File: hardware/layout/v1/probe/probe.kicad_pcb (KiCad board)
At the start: 4 copper layers, 14 x 50 mm, 19 parts, among them J1 Main board, J2 Reflector T-Socket SMD, Q1 AO3400A, U1 SCD41-D-R2, U2 SGP41-D-R4, U3 SHT45-AD1F-R2, U4 LM393DR2G

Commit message: Update documentation to reflect hardware specification changes and component substitutions
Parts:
- U3: value SHT45-AD1F-R2 -> SHT40-AD1F-R2

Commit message: Add silkscreen connector labels to all PCB variants for improved assembly identification
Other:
- board text added: "MAIN"
- board text added: "REFLECTOR"

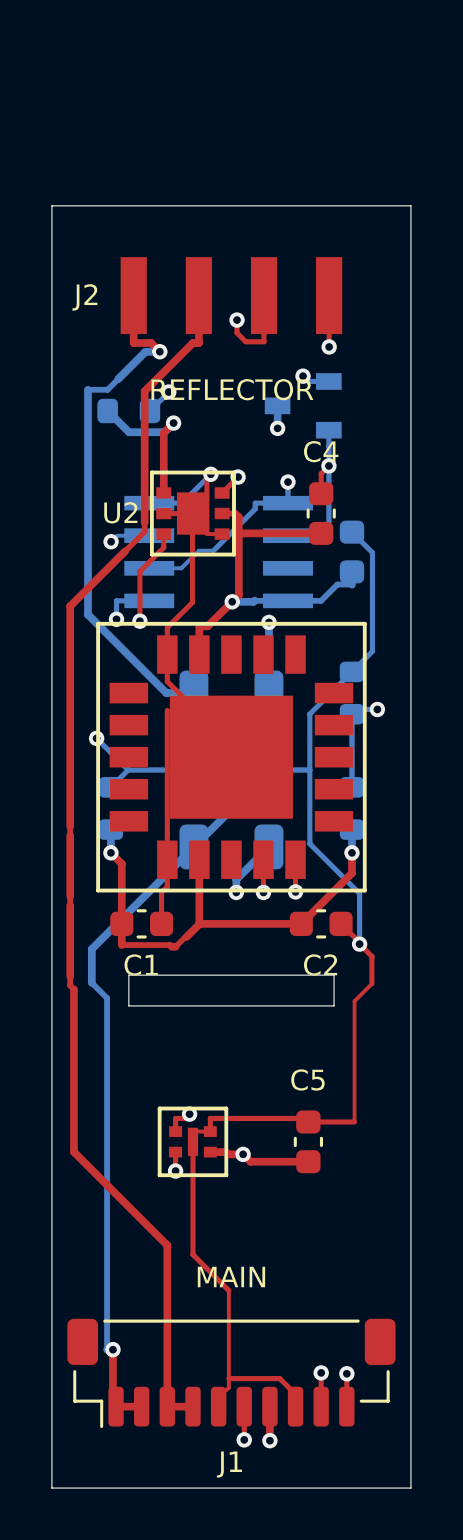
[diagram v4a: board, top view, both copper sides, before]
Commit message: Update enclosure dimensions, add power board, upgrade sensors, and redesign base bay for PMSA003I particulate module
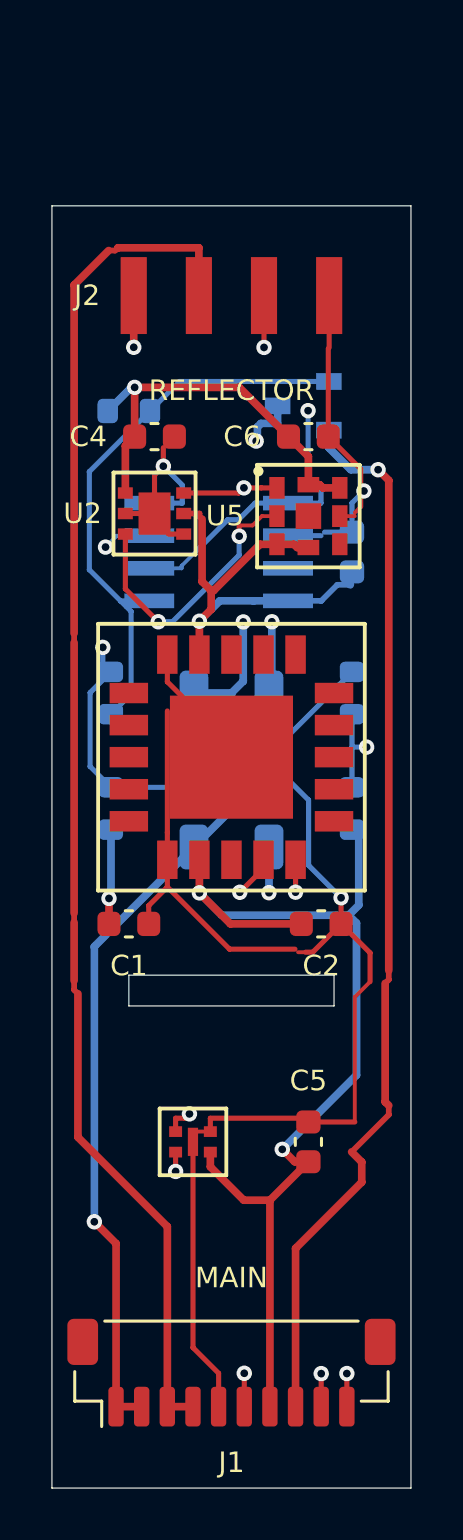
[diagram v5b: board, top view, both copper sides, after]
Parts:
- added C6: 100n 50V, Capacitor_SMD:C_0603_1608Metric, F.Cu at (10.0, -41.0)
- added R7: 470k, Resistor_SMD:R_0603_1608Metric, B.Cu at (2.30, -31.0)
- added U5: BMP585, gateway_fp:Bosch_BMP585_LGA-9, F.Cu at (10.0, -37.9)
- R1, R2: value 470R -> 120R
- moved C4 7.16 mm to (4.00, -41.0), turned to 0 degrees
- moved U2 1.50 mm to (4.00, -38.0)
- moved C1 0.50 mm to (3.00, -22.0)
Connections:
- net VIN_PROT renamed +5V_HEAT
- J1 pad 8: GND -> CO2_HEAT_RTN
- Q1 pad 2: GND -> CO2_HEAT_RTN
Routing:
- net CO2_HEAT_RTN: track 0.00 -> 41.6 mm, vias 0 -> 1
- net I2C_SDA: track 49.8 -> 61.3 mm, vias 4 -> 5
- net I2C_SCL: track 51.0 -> 58.9 mm
- net CO2_VSET: track 21.6 -> 29.1 mm
- net CO2_HEAT_SW: track 34.0 -> 28.0 mm
- net HEAT_SW: track 48.1 -> 53.6 mm
- net +3V3: track 105.7 -> 103.0 mm, vias 6 -> 5
- net NTC_SENSE: track 55.9 -> 53.6 mm
- net +5V_HEAT: track 52.8 -> 53.7 mm, vias 2 -> 3
- net CO2_NTC: track 15.4 -> 16.3 mm
- net GND: track 79.4 -> 78.7 mm, vias 4 -> 3
- net CO2_GATE: track 23.1 -> 22.4 mm, vias 3 -> 0

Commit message: Update documentation for 60V power system, STM32 crown board, 12V heaters, and expanded enclosure design
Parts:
- R1, R2: value 120R -> 680R
- U4: value LM393DR2G -> LM2903DR2G
- moved J2 6.00 mm to (7.00, -52.5)
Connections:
- C3 pad 1: +3V3 -> +12V_HEAT
- J1 pad 1: +5V_HEAT -> +12V_HEAT
- J1 pad 2: +5V_HEAT -> +12V_HEAT
- J2 pad 1: +5V_HEAT -> +12V_HEAT
- R1 pad 1: +5V_HEAT -> +12V_HEAT
- R2 pad 1: +5V_HEAT -> +12V_HEAT
- U4 pad 8: +3V3 -> +12V_HEAT
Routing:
- net +12V_HEAT: track 0.00 -> 63.3 mm, vias 0 -> 3
- net +5V_HEAT: track 53.7 -> 0.00 mm, vias 3 -> 0
- net GND: track 78.7 -> 97.4 mm, vias 3 -> 4
- net I2C_SCL: track 58.9 -> 75.6 mm
- net +3V3: track 103.0 -> 114.4 mm
- net CO2_HEAT_SW: track 28.0 -> 18.1 mm, vias 3 -> 2
- net CO2_VSET: track 29.1 -> 24.1 mm, vias 2 -> 0
- net CO2_GATE: track 22.4 -> 27.2 mm, vias 0 -> 2
- net NTC_SENSE: track 53.6 -> 56.1 mm
- net I2C_SDA: track 61.3 -> 62.3 mm
- net CO2_HEAT_RTN: track 41.6 -> 41.2 mm, vias 1 -> 2
- net CO2_NTC: track 16.3 -> 16.2 mm, vias 2 -> 0
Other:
- board size 14 x 50 mm -> 14 x 56 mm
- board text added: "REFL"
- board text removed: "REFLECTOR"

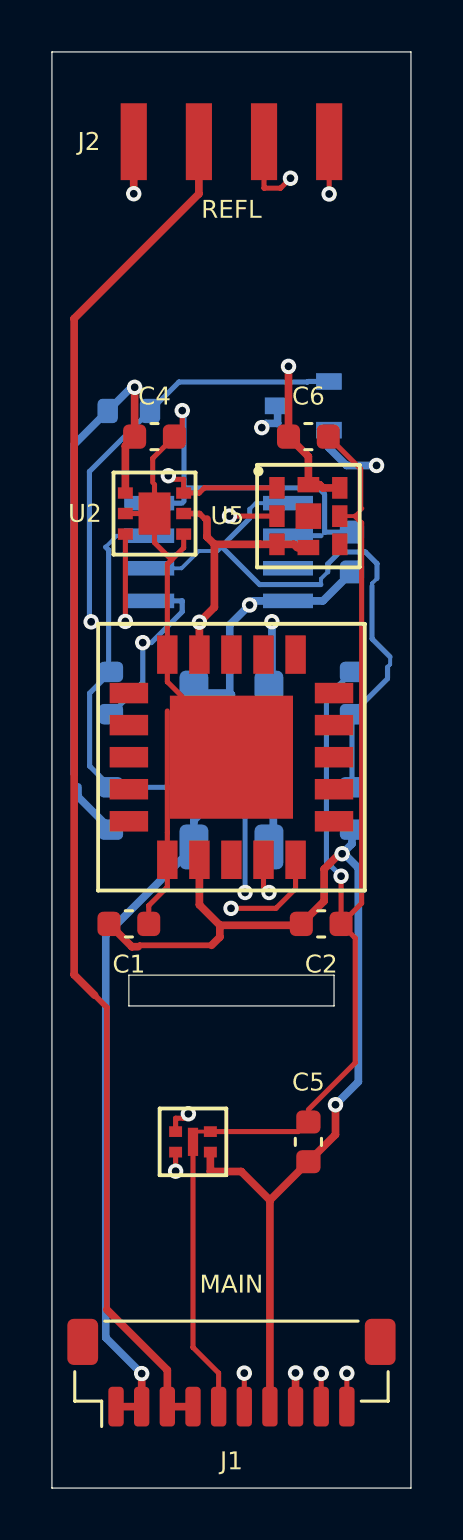
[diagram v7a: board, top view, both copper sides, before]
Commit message: Update documentation for column-packed breakaway panel, probe LDO rail, mast clamp dimensions, transducer adapter redesign, crown SWD/auto-flash workflow, and enclosure print plate organization
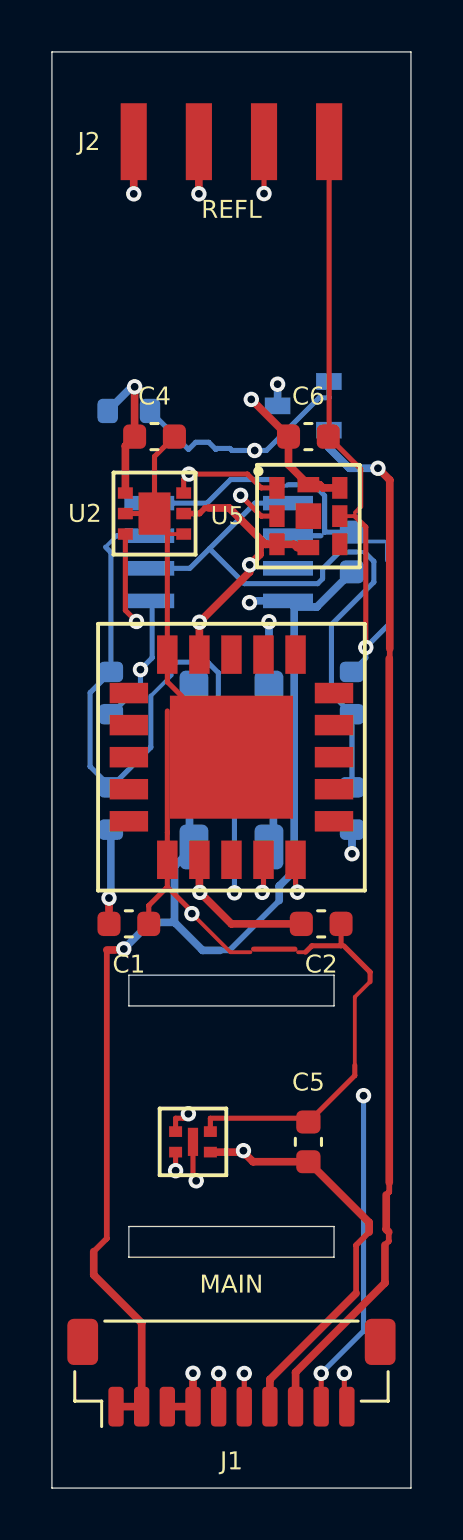
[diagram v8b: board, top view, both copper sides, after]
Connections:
- net +3V3 renamed +3V3_PROBE
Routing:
- net +3V3_PROBE: track 114.4 -> 95.4 mm, vias 5 -> 8
- net +12V_HEAT: track 63.3 -> 81.4 mm
- net I2C_SCL: track 75.6 -> 59.3 mm
- net I2C_SDA: track 62.3 -> 73.7 mm, vias 5 -> 6
- net GND: track 97.4 -> 87.5 mm, vias 4 -> 5
- net CO2_NTC: track 16.2 -> 23.8 mm
- net CO2_GATE: track 27.2 -> 25.5 mm
- net CO2_HEAT_SW: track 18.1 -> 19.5 mm
- net NTC_SENSE: track 56.1 -> 57.2 mm
- net HEAT_SW: track 53.8 -> 54.3 mm, vias 0 -> 2
- net CO2_HEAT_RTN: track 41.2 -> 41.3 mm, vias 2 -> 1
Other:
- outline, holes or cut-outs redrawn
